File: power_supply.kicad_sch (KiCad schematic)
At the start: 44 parts, among them Q1201 IPD50P04P413ATMA2, U1201 LM53603, U1202 LD1117S50TR_SOT223, U1203 LD1117S50TR_SOT223, U1204 LD1117S33TR_SOT223

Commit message: completed schematic
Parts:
- added D508 (x5): GREEN, LED_SMD:LED_0603_1608Metric, symbol Device:LED
- added R524 (x2): 10k, Resistor_SMD:R_0603_1608Metric, symbol Device:R
- added R525, R526, R527: 1k, Resistor_SMD:R_0603_1608Metric, symbol Device:R
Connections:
- net +3.3V: now also R527.2
- net +5V: now also R526.2
- net +5VA: now also R525.2
- net +BATT: now also R524.2
- net GND: now also D508.1 (K), D508.1 (K), D508.1 (K), D508.1 (K), D508.1 (K)
- net Vdrive: now also R524.2
- new net: D508.2 (A), R524.1 (x2)
- new net: D508.2 (A), R527.1
- new net: D508.2 (A), R525.1
- new net: D508.2 (A), R526.1

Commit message: placed components and began routing
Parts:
- C1201: footprint (none) -> Capacitor_SMD:C_0805_2012Metric
- C1203, C1204, C1205, C1213, C1215, C1217: footprint (none) -> Capacitor_SMD:C_1210_3225Metric
- C1210: footprint (none) -> Capacitor_SMD:C_1206_3216Metric
- F1201, F1202, F1203, F1204, F1205, F1206: footprint (none) -> Fuse:Fuse_1206_3216Metric
- L1201: footprint (none) -> Inductor_SMD:L_Bourns_SRP7028A_7.3x6.6mm
- R1202: footprint (none) -> Resistor_SMD:R_0603_1608Metric
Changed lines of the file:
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@@
       (effects (font (size 1.27 1.27)) (justify left))
     )
-    (property "Footprint" "" (at 242.2652 40.64 0)
+    (property "Footprint" "Capacitor_SMD:C_1210_3225Metric" (at 242.2652 40.64 0)
       (effects (font (size 1.27 1.27)) hide)
     )
@@
       (effects (font (size 1.27 1.27)))
     )
-    (property "Footprint" "" (at 40.64 112.522 90)
+    (property "Footprint" "Fuse:Fuse_1206_3216Metric" (at 40.64 112.522 90)
       (effects (font (size 1.27 1.27)) hide)
     )
@@
       (effects (font (size 1.27 1.27)))
     )
-    (property "Footprint" "" (at 69.85 26.162 90)
+    (property "Footprint" "Fuse:Fuse_1206_3216Metric" (at 69.85 26.162 90)
       (effects (font (size 1.27 1.27)) hide)
     )
@@
       (effects (font (size 1.27 1.27)) (justify left))
     )
-    (property "Footprint" "" (at 178.7652 149.86 0)
+    (property "Footprint" "Capacitor_SMD:C_1210_3225Metric" (at 178.7652 149.86 0)
       (effects (font (size 1.27 1.27)) hide)
     )
@@
       (effects (font (size 1.27 1.27)) (justify left))
     )
-    (property "Footprint" "" (at 64.4652 149.86 0)
+    (property "Footprint" "Capacitor_SMD:C_1210_3225Metric" (at 64.4652 149.86 0)
       (effects (font (size 1.27 1.27)) hide)
     )
@@
       (effects (font (size 1.27 1.27)) (justify left))
     )
-    (property "Footprint" "" (at 239.7252 149.86 0)
+    (property "Footprint" "Capacitor_SMD:C_1210_3225Metric" (at 239.7252 149.86 0)
       (effects (font (size 1.27 1.27)) hide)
     )
@@
       (effects (font (size 1.27 1.27)))
     )
-    (property "Footprint" "" (at 198.12 44.958 90)
+    (property "Footprint" "Resistor_SMD:R_0603_1608Metric" (at 198.12 44.958 90)
       (effects (font (size 1.27 1.27)) hide)
     )
@@
       (effects (font (size 1.27 1.27)))
     )
-    (property "Footprint" "" (at 69.85 61.722 90)
+    (property "Footprint" "Fuse:Fuse_1206_3216Metric" (at 69.85 61.722 90)
       (effects (font (size 1.27 1.27)) hide)
     )
@@
       (effects (font (size 1.27 1.27)) (justify left))
     )
-    (property "Footprint" "" (at 254.9652 40.64 0)
+    (property "Footprint" "Capacitor_SMD:C_1210_3225Metric" (at 254.9652 40.64 0)
       (effects (font (size 1.27 1.27)) hide)
     )
@@
       (effects (font (size 1.27 1.27)) (justify left))
     )
-    (property "Footprint" "" (at 127.9652 57.15 0)
+    (property "Footprint" "Capacitor_SMD:C_1206_3216Metric" (at 127.9652 57.15 0)
       (effects (font (size 1.27 1.27)) hide)
     )
@@
       (effects (font (size 1.27 1.27)))
     )
-    (property "Footprint" "" (at 198.12 27.94 0)
+    (property "Footprint" "Inductor_SMD:L_Bourns_SRP7028A_7.3x6.6mm" (at 198.12 27.94 0)
       (effects (font (size 1.27 1.27)) hide)
     )
@@
       (effects (font (size 1.27 1.27)))
     )
-    (property "Footprint" "" (at 247.65 141.478 90)
+    (property "Footprint" "Fuse:Fuse_1206_3216Metric" (at 247.65 141.478 90)
       (effects (font (size 1.27 1.27)) hide)
     )
@@
       (effects (font (size 1.27 1.27)))
     )
-    (property "Footprint" "" (at 187.96 137.922 90)
+    (property "Footprint" "Fuse:Fuse_1206_3216Metric" (at 187.96 137.922 90)
       (effects (font (size 1.27 1.27)) hide)
     )
@@
       (effects (font (size 1.27 1.27)))
     )
-    (property "Footprint" "" (at 72.39 141.478 90)
+    (property "Footprint" "Fuse:Fuse_1206_3216Metric" (at 72.39 141.478 90)
       (effects (font (size 1.27 1.27)) hide)
     )
@@
       (effects (font (size 1.27 1.27)) (justify left))
     )
-    (property "Footprint" "" (at 267.6652 40.64 0)
+    (property "Footprint" "Capacitor_SMD:C_1210_3225Metric" (at 267.6652 40.64 0)
       (effects (font (size 1.27 1.27)) hide)
     )
@@
       (effects (font (size 1.27 1.27)))
     )
-    (property "Footprint" "" (at 185.42 32.0548 0)
-      (effects (font (size 1.27 1.27)) hide)
-    )
+    (property "Footprint" "Capacitor_SMD:C_0805_2012Metric" (at 185.42 32.0548 0)
+      (effects (font (size 1.27 1.27)) hide)
+    )

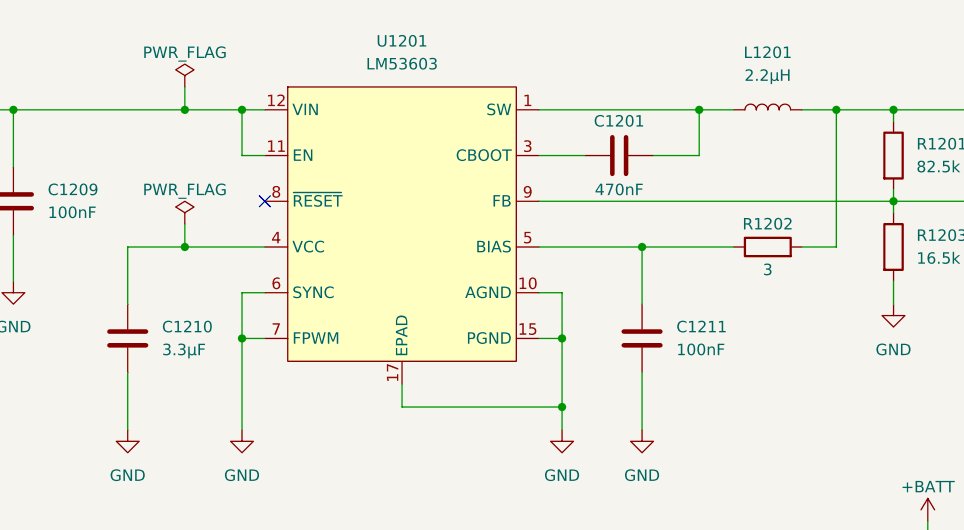
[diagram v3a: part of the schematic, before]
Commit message: fixed oscillator and component values
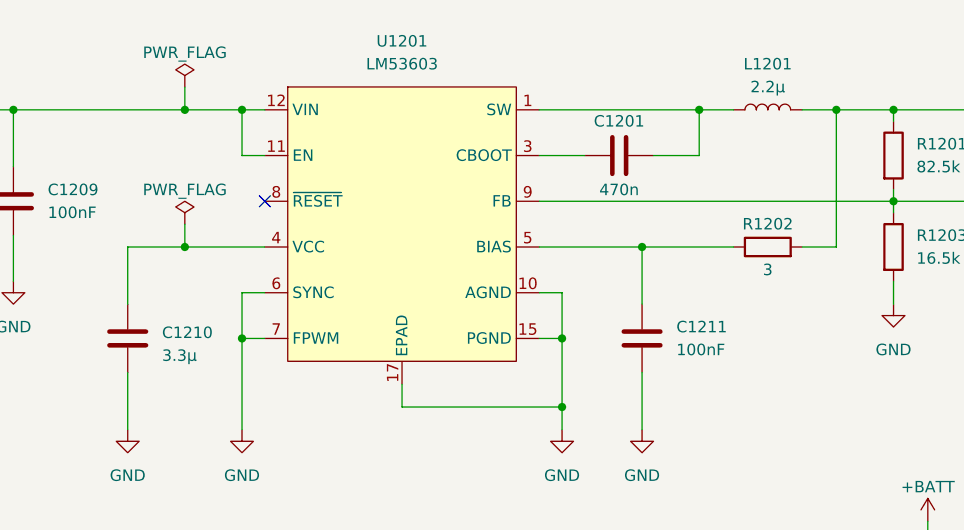
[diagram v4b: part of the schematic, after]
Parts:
- C1201: value 470nF -> 470n
- C1202, C1209, C1211: footprint Resistor_SMD:R_0603_1608Metric -> Capacitor_SMD:C_0603_1608Metric
- C1210: value 3.3µF -> 3.3µ
- L1201: value 2.2µH -> 2.2µ
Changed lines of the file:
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@@
       (effects (font (size 1.27 1.27)) (justify left))
     )
-    (property "Footprint" "Resistor_SMD:R_0603_1608Metric" (at 225.7552 36.83 0)
+    (property "Footprint" "Capacitor_SMD:C_0603_1608Metric" (at 225.7552 36.83 0)
       (effects (font (size 1.27 1.27)) hide)
     )
@@
       (effects (font (size 1.27 1.27)) (justify left))
     )
-    (property "Footprint" "Resistor_SMD:R_0603_1608Metric" (at 185.1152 57.15 0)
+    (property "Footprint" "Capacitor_SMD:C_0603_1608Metric" (at 185.1152 57.15 0)
       (effects (font (size 1.27 1.27)) hide)
     )
@@
   (symbol (lib_id "Device:C") (at 127 53.34 0) (unit 1)
     (in_bom yes) (on_board yes) (dnp no) (fields_autoplaced)
-    (property "Reference" "C1210" (at 130.81 52.0699 0)
-      (effects (font (size 1.27 1.27)) (justify left))
-    )
-    (property "Value" "3.3µF" (at 130.81 54.6099 0)
+    (property "Reference" "C1210" (at 130.81 52.705 0)
+      (effects (font (size 1.27 1.27)) (justify left))
+    )
+    (property "Value" "3.3µ" (at 130.81 55.245 0)
       (effects (font (size 1.27 1.27)) (justify left))
     )
@@
   )
   (symbol (lib_id "Device:L") (at 198.12 27.94 90) (unit 1)
-    (in_bom yes) (on_board yes) (dnp no) (fields_autoplaced)
-    (property "Reference" "L1201" (at 198.12 21.59 90)
-      (effects (font (size 1.27 1.27)))
-    )
-    (property "Value" "2.2µH" (at 198.12 24.13 90)
+    (in_bom yes) (on_board yes) (dnp no)
+    (property "Reference" "L1201" (at 198.12 22.86 90)
+      (effects (font (size 1.27 1.27)))
+    )
+    (property "Value" "2.2µ" (at 198.12 25.4 90)
       (effects (font (size 1.27 1.27)))
     )
@@
       (effects (font (size 1.27 1.27)) (justify left))
     )
-    (property "Footprint" "Resistor_SMD:R_0603_1608Metric" (at 115.2652 41.91 0)
+    (property "Footprint" "Capacitor_SMD:C_0603_1608Metric" (at 115.2652 41.91 0)
       (effects (font (size 1.27 1.27)) hide)
     )
@@
       (effects (font (size 1.27 1.27)))
     )
-    (property "Value" "470nF" (at 181.61 36.83 90)
-      (effects (font (size 1.27 1.27)))
-    )
+    (property "Value" "470n" (at 181.61 36.83 90)
+      (effects (font (size 1.27 1.27)))
+    )

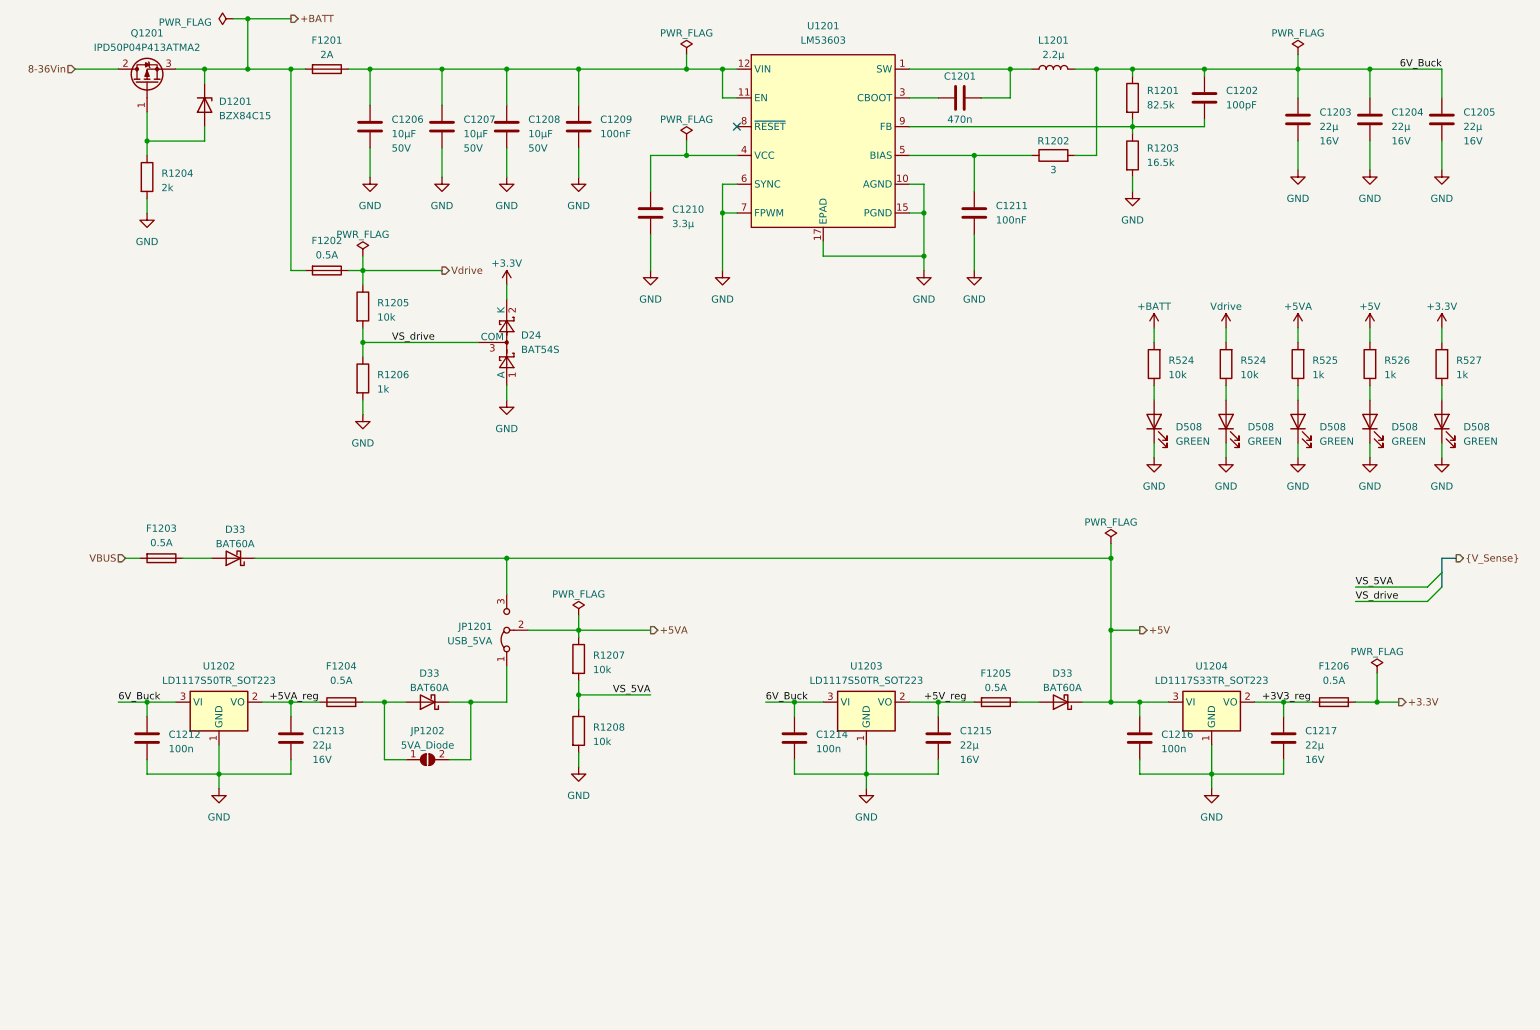
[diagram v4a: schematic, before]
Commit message: hierarchical sheets for digital I/O and replaced power supply jumpers with relays
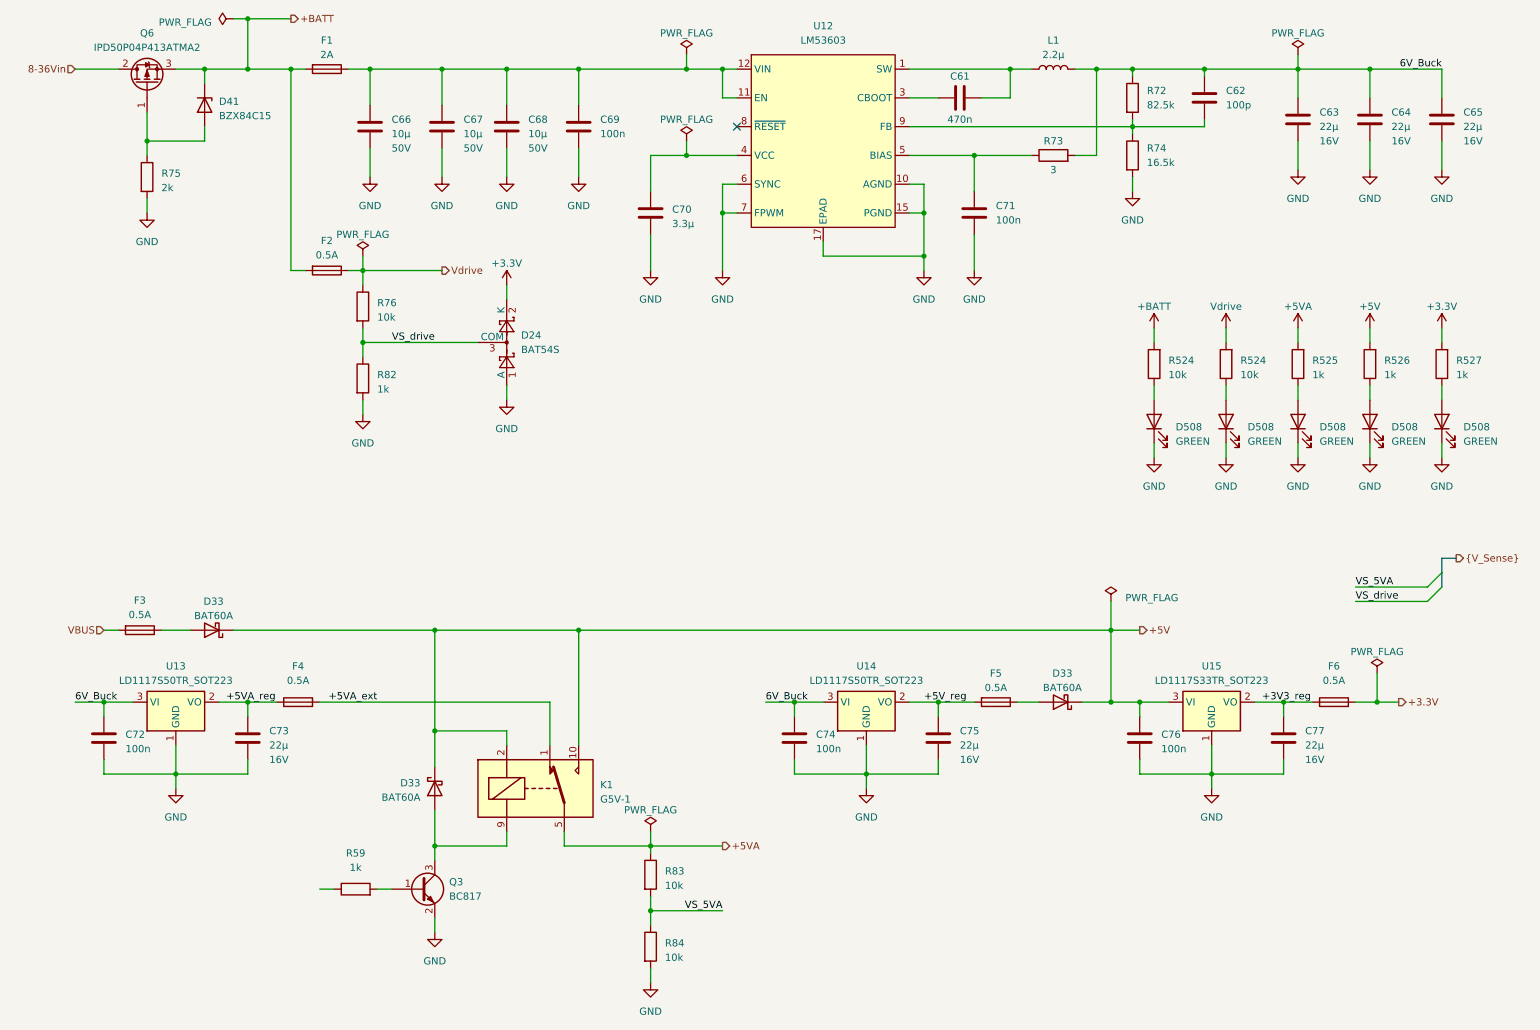
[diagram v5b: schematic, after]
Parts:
- removed JP1201: USB_5VA, Connector_PinHeader_2.54mm:PinHeader_1x03_P2.54mm_Vertical, symbol Jumper:Jumper_3_Bridged12
- removed JP1202: 5VA_Diode, Jumper:SolderJumper-2_P1.3mm_Open_Pad1.0x1.5mm, symbol Jumper:SolderJumper_2_Open
- added K1: G5V-1, Relay_THT:Relay_SPDT_Omron_G5V-1, symbol Relay:G5V-1
- added Q3: BC817, Package_TO_SOT_SMD:SOT-23, symbol FaSTTUBe_PnP:BC817
- added R59: 1k, Resistor_SMD:R_0603_1608Metric, symbol Device:R
- C62: renamed from C1202; value 100pF -> 100p
- C66: renamed from C1206; value 10µF -> 10µ
- C67: renamed from C1207; value 10µF -> 10µ
- C68: renamed from C1208; value 10µF -> 10µ
- C69: renamed from C1209; value 100nF -> 100n
- C71: renamed from C1211; value 100nF -> 100n
- renumbered C1201 to C61, C1203 to C63, C1204 to C64, C1205 to C65, C1210 to C70, C1212 to C72, C1213 to C73, C1214 to C74, C1215 to C75, C1216 to C76, C1217 to C77, D1201 to D41, F1201 to F1, F1202 to F2, F1203 to F3, F1204 to F4, F1205 to F5, F1206 to F6, L1201 to L1, Q1201 to Q6, R1201 to R72, R1202 to R73, R1203 to R74, R1204 to R75, R1205 to R76, R1206 to R82, R1207 to R83, R1208 to R84, U1201 to U12, U1202 to U13, U1203 to U14, U1204 to U15
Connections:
- net +5V: now also D33.1 (K), K1.10, K1.2
- net +5VA: now also K1.5, K1.6
- net GND: now also Q3.2 (E)
- net at D33.2 (A): now also K1.9, Q3.3 (C); no longer F4.2
- new net: Q3.1 (B), R59.2
- new net +5VA_ext: F4.2, K1.1
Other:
- moved on the sheet: C72, C73, D33, F3, F4, R83, R84, U13
